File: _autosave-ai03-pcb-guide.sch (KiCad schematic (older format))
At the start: 2 parts

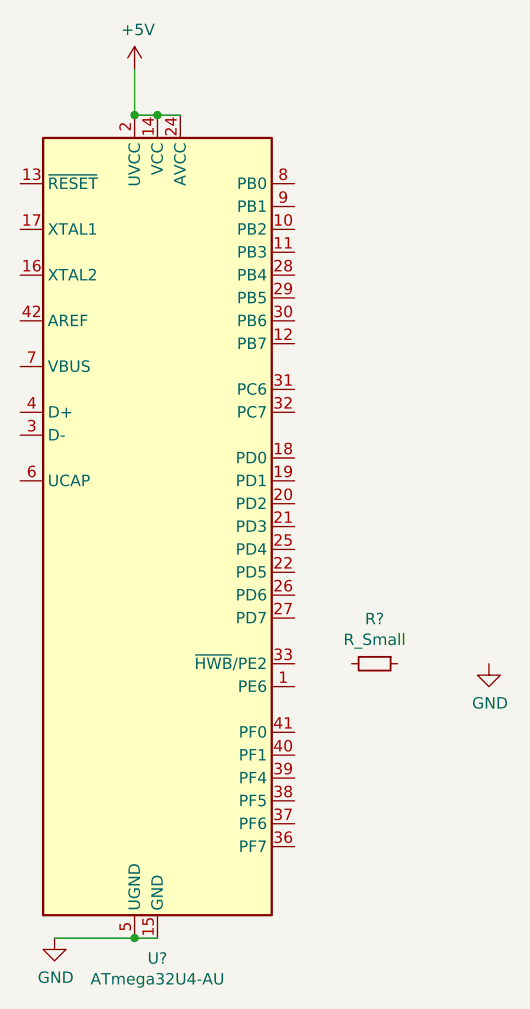
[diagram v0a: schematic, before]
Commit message: added power connections
Need to update R_Small from HWB -> GND
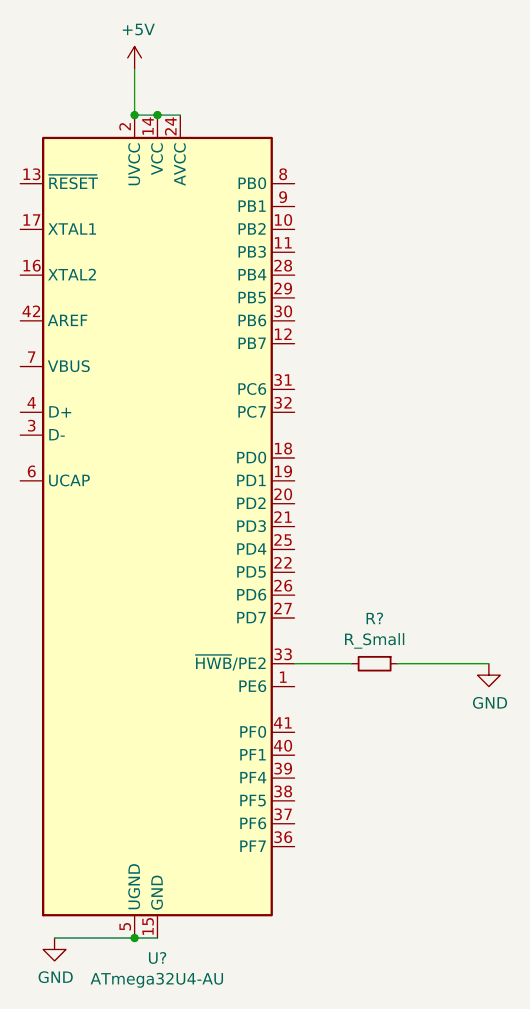
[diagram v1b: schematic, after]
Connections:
- net GND: now also R?.1
- net at U?.33 (~HWB~/PE2): now also R?.2
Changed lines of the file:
@@
 	1    0    0    -1
 $EndComp
+Wire Wire Line
+	3150 4400 3400 4400
+Wire Wire Line
+	3600 4400 4000 4400
 $EndSCHEMATC
